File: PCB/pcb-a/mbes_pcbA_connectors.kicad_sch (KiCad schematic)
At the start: 29 parts, among them J1 Conn_02x05_Counter_Clockwise, J2 Conn_02x05_Counter_Clockwise, Q2 BC807, Q4 BC807, Q5 BC807, Q6 BC807, U3 L7805

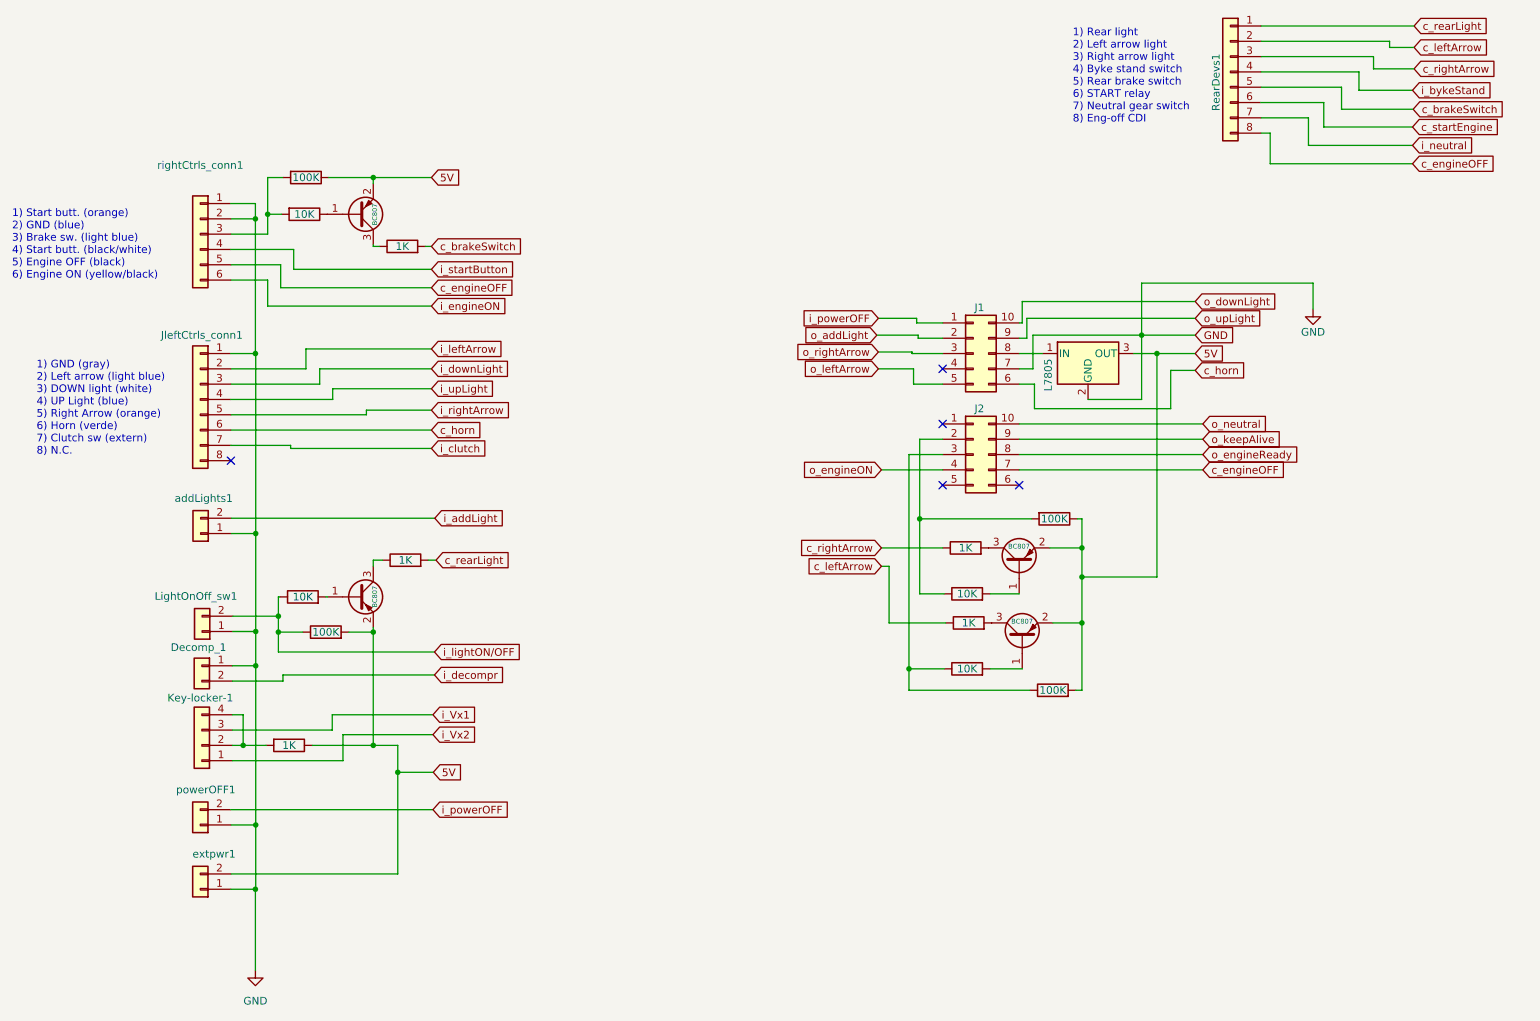
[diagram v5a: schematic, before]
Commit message: Many changes and fixes
Electric schema A & B
	- Wrong (undefined) signals direction fixed
	- More readable schema getting: c_<signal> color has changed
	- Some pull-up resistors has been added for safing purpose
	- Wire connectors holes size reducing
	- Because Led indicatord uses less then 500mA, their wire connectors have been substituted by pin-header ones

PCB
	- Updates for schema changes
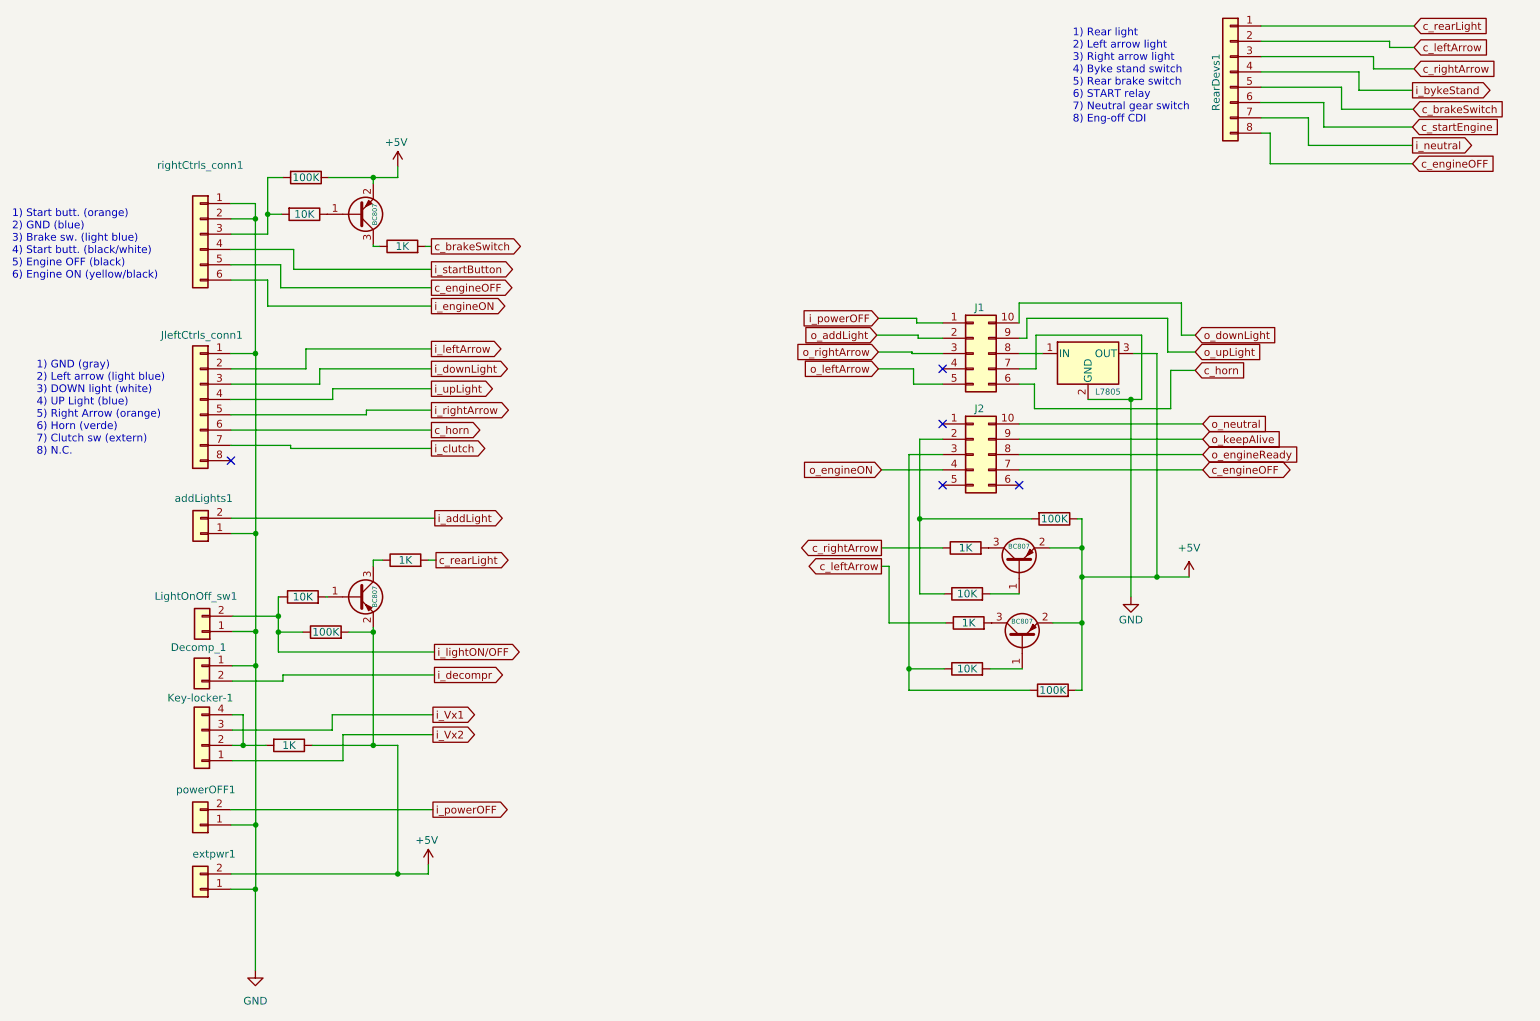
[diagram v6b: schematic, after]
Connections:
- net 5V renamed +5V

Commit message: Small changes for the Title block
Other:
- company: Panicosoft -> https://github.com/catinella/mbElectricalSystem
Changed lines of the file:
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@@
 	(title_block
 		(title "All the pcb's connectors")
-		(rev "4.0")
-		(company "Panicosoft")
+		(company "https://github.com/catinella/mbElectricalSystem")
 	)
 	(text "1) Start butt. (orange)\n2) GND (blue)\n3) Brake sw. (light blue)\n4) Start butt. (black/white)\n5) Engine OFF (black)\n6) Engine ON (yellow/black)"
